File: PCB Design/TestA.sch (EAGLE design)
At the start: 52 parts, among them IC1 SI7021, IC2 ATMEGA328-PB, IC3 PE4259, U1 V_REG_317SMD, U2 LSM9DS1, Y1 16MHz, Y2 32Mhz

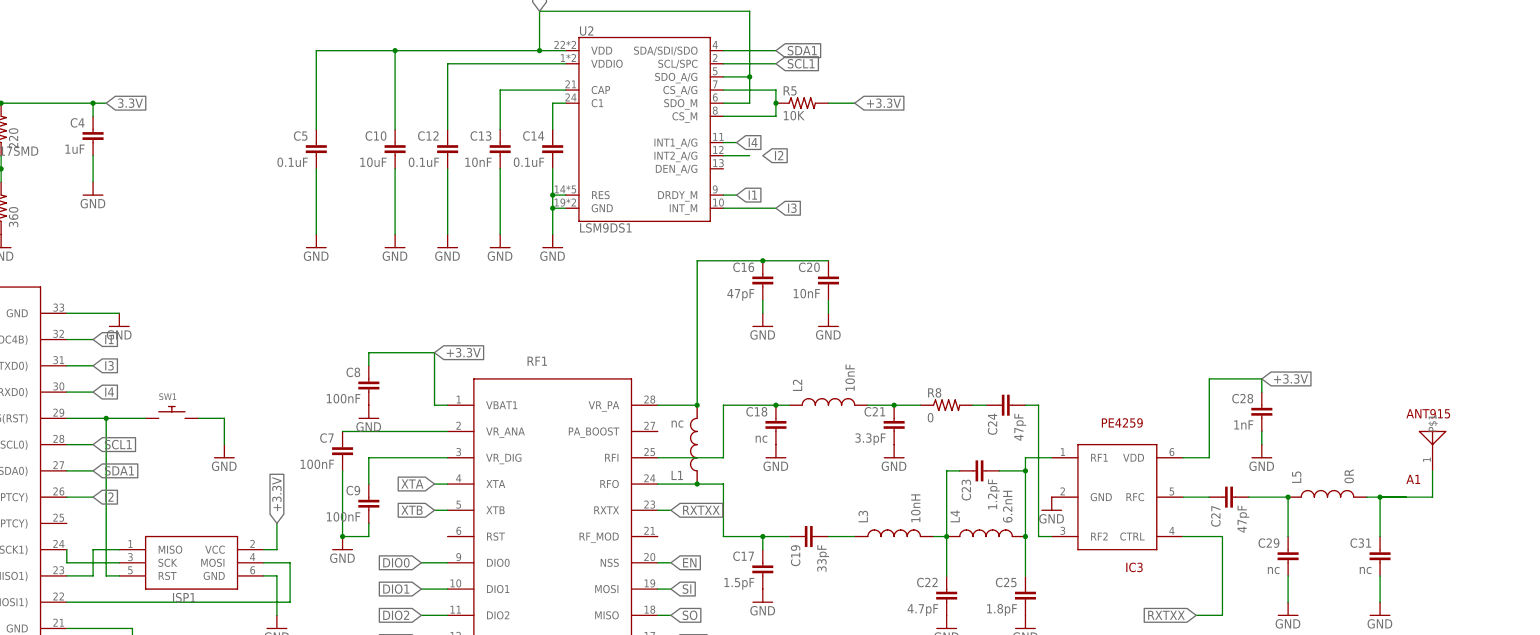
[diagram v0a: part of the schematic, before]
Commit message: Removed SMD Antenna and made a few other changes after preliminary QA
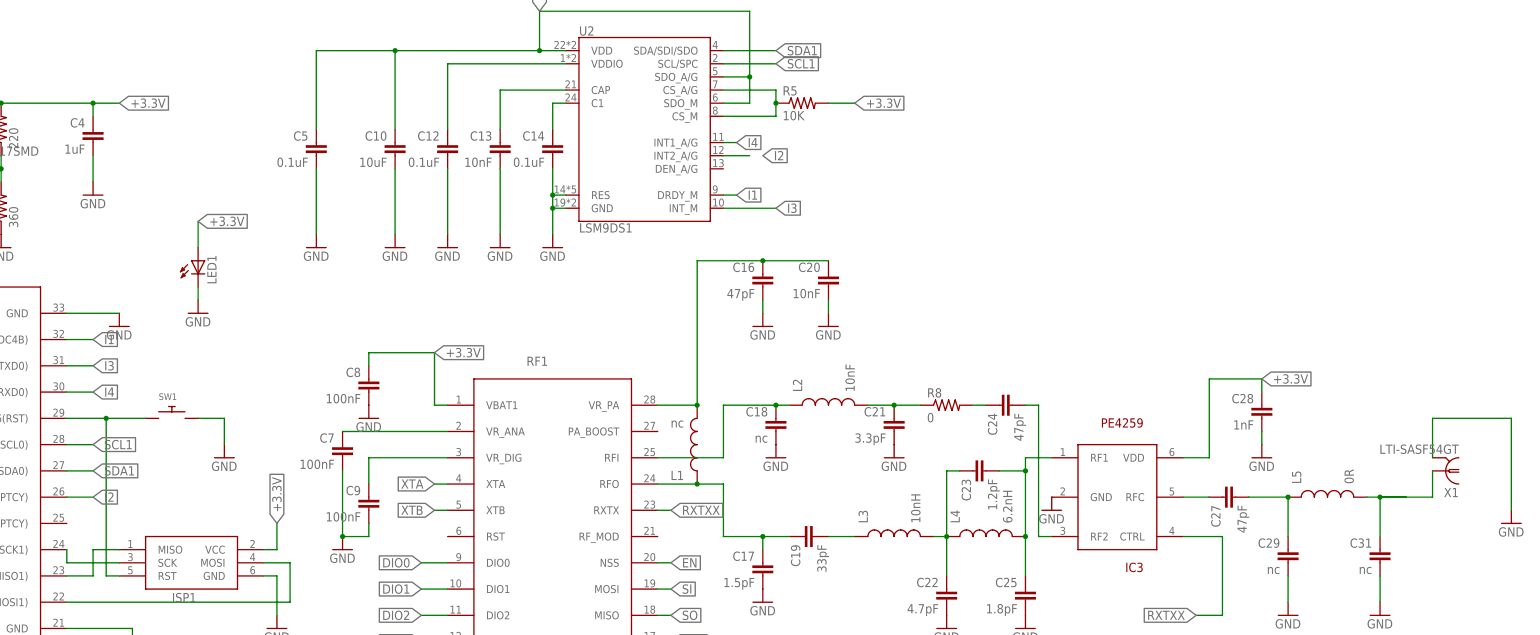
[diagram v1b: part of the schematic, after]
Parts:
- removed A1: ANT915, Mini-Project:ANT915
- added LED1: (no value), adafruit:LED3MM
- added X1: LTI-SASF54GT, con-coax:LTI-SASF54GT
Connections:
- removed net 3.3V: C4.1, R3.2, U1.OUT
- net +3.3V: now also C4.1, LED1.A, R3.2, U1.OUT
- net GND: now also LED1.C, X1.2
- net N$15: now also X1.1; no longer A1.P$1
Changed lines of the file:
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@@
 <part name="GND10" library="supply1" library_urn="urn:adsk.eagle:library:371" deviceset="GND" device=""/>
 <part name="Y2" library="SparkFun-Clocks" deviceset="CRYSTAL-16MHZ" device="SMD-2X1.6" value="32Mhz"/>
-<part name="A1" library="Mini-Project" deviceset="ANT915" device=""/>
 <part name="IC3" library="Mini-Project" deviceset="PE4259" device=""/>
 <part name="L2" library="SparkFun" deviceset="INDUCTOR" device="0402" value="10nF"/>
@@
 <part name="ISP1" library="adafruit" deviceset="AVRISP" device="-6"/>
 <part name="GND36" library="supply1" library_urn="urn:adsk.eagle:library:371" deviceset="GND" device=""/>
+<part name="GND24" library="supply1" library_urn="urn:adsk.eagle:library:371" deviceset="GND" device=""/>
+<part name="X1" library="con-coax" library_urn="urn:adsk.eagle:library:133" deviceset="LTI-SASF54GT" device="" package3d_urn="urn:adsk.eagle:package:6232/1"/>
+<part name="LED1" library="adafruit" deviceset="LED" device="3MM"/>
+<part name="GND26" library="SparkFun" deviceset="GND" device=""/>
 </parts>
 <sheets>
@@
 <attribute name="VALUE" x="157.48" y="0.508" size="1.778" layer="96" font="vector" align="top-center"/>
 </instance>
-<instance part="A1" gate="G$1" x="363.22" y="55.88" smashed="yes">
-<attribute name="NAME" x="358.14" y="50.8" size="1.778" layer="94"/>
-<attribute name="VALUE" x="358.14" y="63.5" size="1.778" layer="94"/>
-</instance>
 <instance part="IC3" gate="G$1" x="302.26" y="48.26" smashed="yes" rot="R180">
 <attribute name="NAME" x="307.34" y="35.56" size="1.778" layer="94" rot="R180"/>
@@
 <instance part="GND36" gate="1" x="139.7" y="22.86" smashed="yes">
 <attribute name="VALUE" x="137.16" y="20.32" size="1.778" layer="96"/>
+</instance>
+<instance part="GND24" gate="1" x="378.46" y="43.18" smashed="yes">
+<attribute name="VALUE" x="375.92" y="40.64" size="1.778" layer="96"/>
+</instance>
+<instance part="X1" gate="G$1" x="365.76" y="53.34" smashed="yes" rot="R180">
+<attribute name="VALUE" x="368.3" y="58.42" size="1.778" layer="96" rot="R180"/>
+<attribute name="NAME" x="368.3" y="50.038" size="1.778" layer="95" rot="R180"/>
+</instance>
+<instance part="LED1" gate="G$1" x="124.46" y="93.98" smashed="yes">
+<attribute name="NAME" x="128.016" y="89.408" size="1.778" layer="95" rot="R90"/>
+<attribute name="VALUE" x="130.175" y="89.408" size="1.778" layer="96" rot="R90"/>
+</instance>
+<instance part="GND26" gate="1" x="124.46" y="83.82" smashed="yes">
+<attribute name="VALUE" x="121.92" y="81.28" size="1.778" layer="96"/>
 </instance>
 </instances>
@@
 <wire x1="139.7" y1="33.02" x2="139.7" y2="25.4" width="0.1524" layer="91"/>
 <pinref part="GND36" gate="1" pin="GND"/>
+</segment>
+<segment>
+<pinref part="X1" gate="G$1" pin="2"/>
+<wire x1="363.22" y1="55.88" x2="363.22" y2="63.5" width="0.1524" layer="91"/>
+<pinref part="GND24" gate="1" pin="GND"/>
+<wire x1="363.22" y1="63.5" x2="378.46" y2="63.5" width="0.1524" layer="91"/>
+<wire x1="378.46" y1="63.5" x2="378.46" y2="45.72" width="0.1524" layer="91"/>
+</segment>
+<segment>
+<pinref part="GND26" gate="1" pin="GND"/>
+<pinref part="LED1" gate="G$1" pin="C"/>
+<wire x1="124.46" y1="86.36" x2="124.46" y2="88.9" width="0.1524" layer="91"/>
 </segment>
 </net>
@@
 <label x="139.7" y="43.18" size="1.778" layer="95" rot="R90" xref="yes"/>
 </segment>
+<segment>
+<pinref part="U1" gate="G$1" pin="OUT"/>
+<wire x1="81.28" y1="124.46" x2="86.36" y2="124.46" width="0.1524" layer="91"/>
+<label x="109.22" y="124.46" size="1.778" layer="95" xref="yes"/>
+<pinref part="R3" gate="G$1" pin="2"/>
+<wire x1="86.36" y1="124.46" x2="104.14" y2="124.46" width="0.1524" layer="91"/>
+<junction x="86.36" y="124.46"/>
+<pinref part="C4" gate="G$1" pin="1"/>
+<wire x1="104.14" y1="124.46" x2="109.22" y2="124.46" width="0.1524" layer="91"/>
+<wire x1="104.14" y1="121.92" x2="104.14" y2="124.46" width="0.1524" layer="91"/>
+<junction x="104.14" y="124.46"/>
+</segment>
+<segment>
+<pinref part="LED1" gate="G$1" pin="A"/>
+<wire x1="124.46" y1="96.52" x2="124.46" y2="101.6" width="0.1524" layer="91"/>
+<label x="124.46" y="101.6" size="1.778" layer="95" xref="yes"/>
+</segment>
 </net>
 <net name="N$17" class="0">
@@
 <pinref part="R5" gate="G$1" pin="1"/>
 <junction x="236.22" y="124.46"/>
-</segment>
-</net>
-<net name="3.3V" class="0">
-<segment>
-<pinref part="U1" gate="G$1" pin="OUT"/>
-<wire x1="81.28" y1="124.46" x2="86.36" y2="124.46" width="0.1524" layer="91"/>
-<label x="106.68" y="124.46" size="1.778" layer="95" xref="yes"/>
-<pinref part="R3" gate="G$1" pin="2"/>
-<wire x1="86.36" y1="124.46" x2="104.14" y2="124.46" width="0.1524" layer="91"/>
-<junction x="86.36" y="124.46"/>
-<pinref part="C4" gate="G$1" pin="1"/>
-<wire x1="104.14" y1="124.46" x2="106.68" y2="124.46" width="0.1524" layer="91"/>
-<wire x1="104.14" y1="121.92" x2="104.14" y2="124.46" width="0.1524" layer="91"/>
-<junction x="104.14" y="124.46"/>
 </segment>
 </net>
@@
 <wire x1="353.06" y1="40.64" x2="353.06" y2="48.26" width="0.1524" layer="91"/>
 <junction x="353.06" y="48.26"/>
-<pinref part="A1" gate="G$1" pin="P$1"/>
 <wire x1="363.22" y1="48.26" x2="363.22" y2="53.34" width="0.1524" layer="91"/>
 <wire x1="353.06" y1="48.26" x2="363.22" y2="48.26" width="0.1524" layer="91"/>
+<pinref part="X1" gate="G$1" pin="1"/>
 </segment>
 </net>
@@
 will not be understood (or retained) with this version.
 </note>
+<note version="8.3" severity="warning">
+Since Version 8.3, EAGLE supports the association of 3D packages
+with devices in libraries, schematics, and board files. Those 3D
+packages will not be understood (or retained) with this version.
+</note>
 </compatibility>
